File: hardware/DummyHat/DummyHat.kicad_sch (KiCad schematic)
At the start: 41 parts, among them J1 Conn_01x08_Socket, J2 Conn_01x08_Socket, J3 Conn_01x08_Socket, Q1 PZT2222A, U1 74HC688, U2 74HC245, U3 74HC245

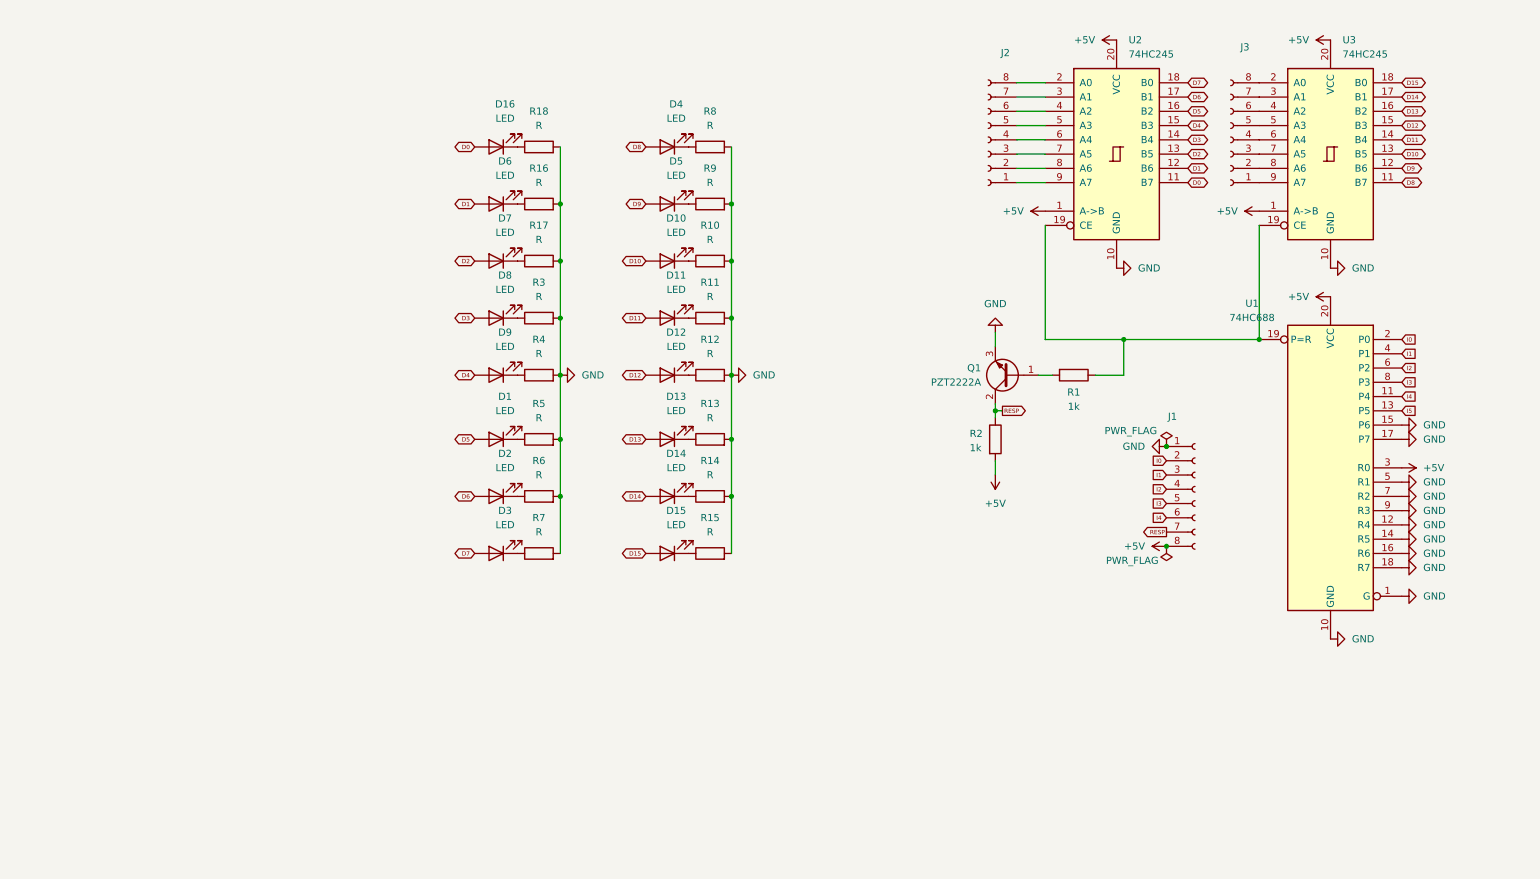
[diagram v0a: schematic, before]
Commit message: changed voltage selector to actually work
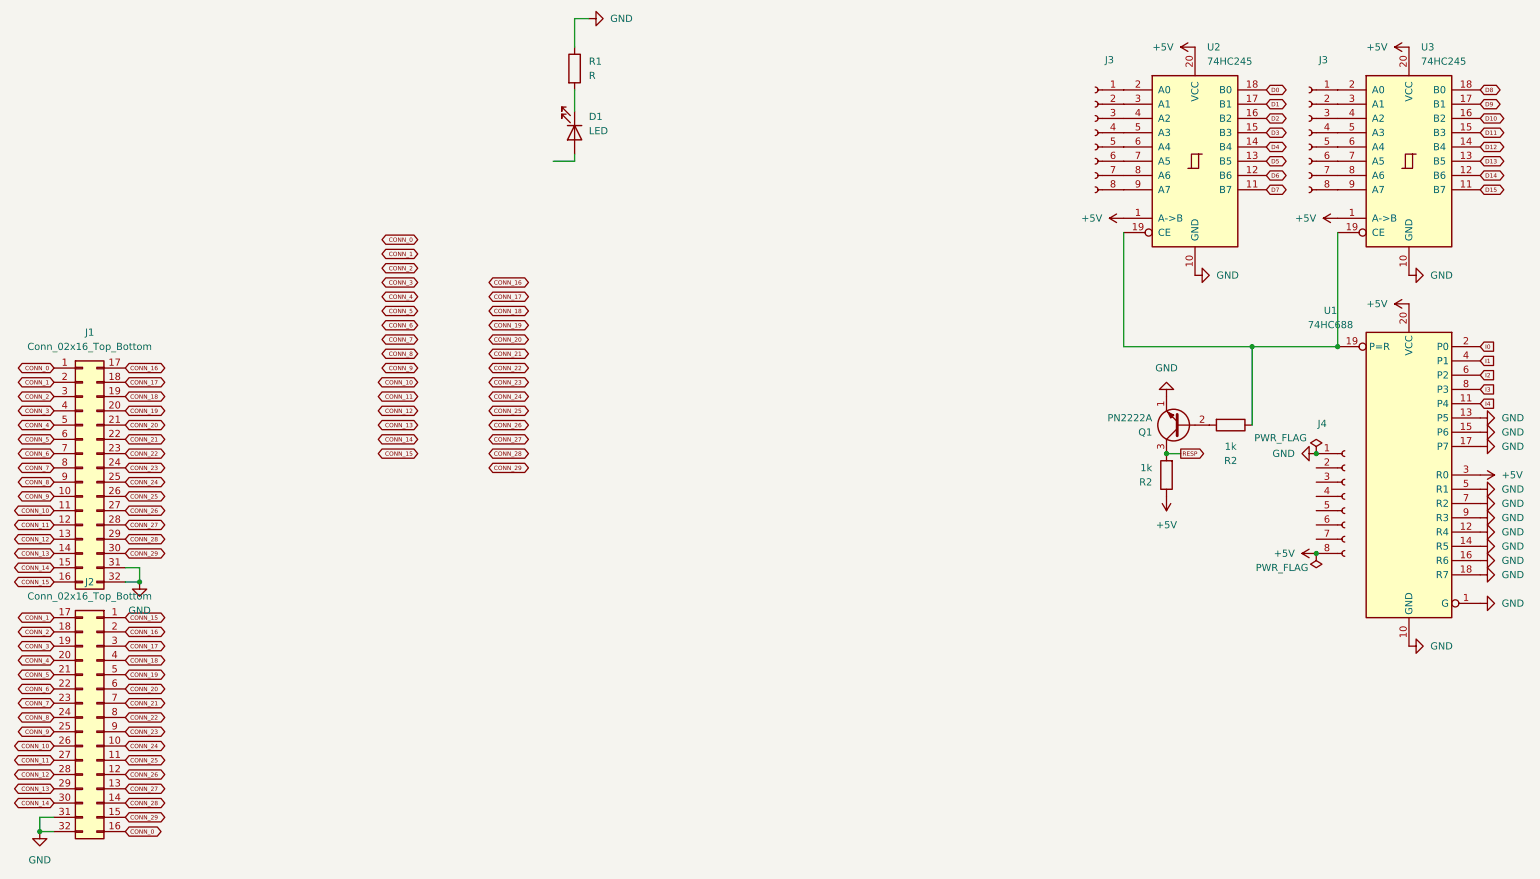
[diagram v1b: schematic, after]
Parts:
- removed D10, D11, D12, D13, D14, D15, D16, D2, D3, D4, D5, D6, D7, D8, D9: LED, LED_SMD:LED_1812_4532Metric_Pad1.30x3.40mm_HandSolder, symbol Device:LED
- removed J1, J2: Conn_01x08_Socket, Connector_PinSocket_2.54mm:PinSocket_1x08_P2.54mm_Vertical, symbol Connector:Conn_01x08_Socket
- removed Q1: PZT2222A, Package_TO_SOT_SMD:SOT-223-3_TabPin2, symbol Transistor_BJT:PZT2222A
- removed R10, R11, R12, R13, R14, R15, R16, R17, R18, R3, R4, R5, R6, R7, R8, R9: R, Resistor_SMD:R_0402_1005Metric, symbol Device:R
- removed R2: 1k, Resistor_SMD:R_0201_0603Metric, symbol Device:R
- added J1: Conn_02x16_Top_Bottom, MolexFSB:FSB5 Series 0.40 mm Pitch Floating SlimStack Board-to-Board Receptacles, symbol Connector_Generic:Conn_02x16_Top_Bottom
- added J2: Conn_02x16_Top_Bottom, MolexFSB:FSB5 Series 0.40 mm Pitch Floating SlimStack Board-to-Board Plugs, symbol Connector_Generic:Conn_02x16_Top_Bottom
- added J3, J4: Conn_01x08_Socket, Connector_PinSocket_2.54mm:PinSocket_1x08_P2.54mm_Vertical, symbol Connector:Conn_01x08_Socket
- added Q1: PN2222A, Package_TO_SOT_THT:TO-92_Inline, symbol Transistor_BJT:PN2222A
- added R2 (x2): 1k, Resistor_THT:R_Axial_DIN0207_L6.3mm_D2.5mm_P10.16mm_Horizontal, symbol Device:R
- D1: footprint LED_SMD:LED_1812_4532Metric_Pad1.30x3.40mm_HandSolder -> LED_SMD:LED_0603_1608Metric
- R1: value 1k -> R; footprint Resistor_SMD:R_0201_0603Metric -> Resistor_SMD:R_0603_1608Metric
- U1, U2, U3: footprint Package_SO:TSSOP-20_4.4x6.5mm_P0.65mm -> Package_DIP:DIP-20_W7.62mm
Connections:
- net I5 is gone; now on net GND: U1.13 (P5)
- net +5V: now also J4.8 (Pin_8), R2.1
- net D0: now also U2.18 (B0); no longer U2.11 (B7)
- net D1: now also U2.17 (B1); no longer U2.12 (B6)
- net D10: now also U3.16 (B2); no longer U3.13 (B5)
- net D11: now also U3.15 (B3); no longer U3.14 (B4)
- net D12: now also U3.14 (B4); no longer U3.15 (B3)
- net D13: now also U3.13 (B5); no longer U3.16 (B2)
- net D14: now also U3.12 (B6); no longer U3.17 (B1)
- net D15: now also U3.11 (B7); no longer U3.18 (B0)
- net D2: now also U2.16 (B2); no longer U2.13 (B5)
- net D3: now also U2.15 (B3); no longer U2.14 (B4)
- net D4: now also U2.14 (B4); no longer U2.15 (B3)
- net D5: now also U2.13 (B5); no longer D1.2 (A), U2.16 (B2)
- net D6: now also U2.12 (B6); no longer U2.17 (B1)
- net D7: now also U2.11 (B7); no longer U2.18 (B0)
- net D8: now also U3.18 (B0); no longer U3.11 (B7)
- net D9: now also U3.17 (B1); no longer U3.12 (B6)
- net GND: now also R1.1, J1.31 (Pin_31), J1.32 (Pin_32), J2.31 (Pin_31), J2.32 (Pin_32), J4.1 (Pin_1), Q1.1 (E)
- net RESP: now also Q1.3 (C), R2.2
- net at U1.19 (P=R), U2.19 (CE), U3.19 (CE): now also R2.1; no longer R1.1
- net at R1.2: now also D1.1 (K)
- net at U2.9 (A7): now also J3.8 (Pin_8)
- net at U2.8 (A6): now also J3.7 (Pin_7)
- net at U2.7 (A5): now also J3.6 (Pin_6)
- net at U2.6 (A4): now also J3.5 (Pin_5)
- net at U2.5 (A3): now also J3.4 (Pin_4)
- net at U2.4 (A2): now also J3.3 (Pin_3)
- net at U2.3 (A1): now also J3.2 (Pin_2)
- net at U2.2 (A0): now also J3.1 (Pin_1)
- net at U3.2 (A0): now also J3.1 (Pin_1); no longer J3.8 (Pin_8)
- net at U3.3 (A1): now also J3.2 (Pin_2); no longer J3.7 (Pin_7)
- net at U3.4 (A2): now also J3.3 (Pin_3); no longer J3.6 (Pin_6)
- net at U3.5 (A3): now also J3.4 (Pin_4); no longer J3.5 (Pin_5)
- net at U3.6 (A4): now also J3.5 (Pin_5); no longer J3.4 (Pin_4)
- net at U3.7 (A5): now also J3.6 (Pin_6); no longer J3.3 (Pin_3)
- net at U3.8 (A6): now also J3.7 (Pin_7); no longer J3.2 (Pin_2)
- net at U3.9 (A7): now also J3.8 (Pin_8); no longer J3.1 (Pin_1)
- new net: Q1.2 (B), R2.2
- new net CONN_0: J1.1 (Pin_1), J2.16 (Pin_16)
- new net CONN_1: J1.2 (Pin_2), J2.17 (Pin_17)
- new net CONN_10: J1.11 (Pin_11), J2.26 (Pin_26)
- new net CONN_11: J1.12 (Pin_12), J2.27 (Pin_27)
- new net CONN_12: J1.13 (Pin_13), J2.28 (Pin_28)
- new net CONN_13: J1.14 (Pin_14), J2.29 (Pin_29)
- new net CONN_14: J1.15 (Pin_15), J2.30 (Pin_30)
- new net CONN_15: J1.16 (Pin_16), J2.1 (Pin_1)
- new net CONN_16: J1.17 (Pin_17), J2.2 (Pin_2)
- new net CONN_17: J1.18 (Pin_18), J2.3 (Pin_3)
- new net CONN_18: J1.19 (Pin_19), J2.4 (Pin_4)
- new net CONN_19: J1.20 (Pin_20), J2.5 (Pin_5)
- new net CONN_2: J1.3 (Pin_3), J2.18 (Pin_18)
- new net CONN_20: J1.21 (Pin_21), J2.6 (Pin_6)
- new net CONN_21: J1.22 (Pin_22), J2.7 (Pin_7)
- new net CONN_22: J1.23 (Pin_23), J2.8 (Pin_8)
- new net CONN_23: J1.24 (Pin_24), J2.9 (Pin_9)
- new net CONN_24: J1.25 (Pin_25), J2.10 (Pin_10)
- new net CONN_25: J1.26 (Pin_26), J2.11 (Pin_11)
- new net CONN_26: J1.27 (Pin_27), J2.12 (Pin_12)
- new net CONN_27: J1.28 (Pin_28), J2.13 (Pin_13)
- new net CONN_28: J1.29 (Pin_29), J2.14 (Pin_14)
- new net CONN_29: J1.30 (Pin_30), J2.15 (Pin_15)
- new net CONN_3: J1.4 (Pin_4), J2.19 (Pin_19)
- new net CONN_4: J1.5 (Pin_5), J2.20 (Pin_20)
- new net CONN_5: J1.6 (Pin_6), J2.21 (Pin_21)
- new net CONN_6: J1.7 (Pin_7), J2.22 (Pin_22)
- new net CONN_7: J1.8 (Pin_8), J2.23 (Pin_23)
- new net CONN_8: J1.9 (Pin_9), J2.24 (Pin_24)
- new net CONN_9: J1.10 (Pin_10), J2.25 (Pin_25)
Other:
- moved on the sheet: J3, U1, U2, U3
